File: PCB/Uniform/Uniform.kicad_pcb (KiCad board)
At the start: 2 copper layers, 156 parts, among them CON1 826629-5, CON2 Conn_01x03, U1 STM32L072KZT6

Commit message: finished board outline
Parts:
- moved R1 19.6 mm to (365.4, 230.5)
- moved R2 19.6 mm to (381.2, 230.5)
- moved R3 19.6 mm to (397.1, 230.5)
- moved R5 19.6 mm to (444.6, 230.5)
- moved R6 19.6 mm to (428.8, 230.5)
- moved C5 19.6 mm to (449.4, 234.9)
- moved CON1 19.6 mm to (366.6, 234.9)
- moved D_3_7 19.6 mm to (384.9, 234.6)
- moved D_4_10 19.6 mm to (407.9, 234.6)
- moved D_4_6 19.6 mm to (442.3, 234.6)
- moved D_4_8 19.6 mm to (430.9, 234.6)
- moved D_4_9 19.6 mm to (419.4, 234.6)
- moved S2 19.6 mm to (465.5, 231.0)
- moved R4 19.6 mm to (412.9, 230.5)
- moved D_0_10 19.6 mm to (396.4, 234.6)
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
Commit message: flipped exposed PCB side to make room for USBC pins
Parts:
- USBC1: moved to B.Cu
- moved USBC1 347.9 mm to (56.5, 107.8)
- moved CON1 343.8 mm to (42.9, 119.1), turned to 90 degrees
- moved K_0_0 26.9 mm to (71.4, 114.3)
- moved K_1_0 26.9 mm to (71.4, 133.3)
- moved K_0_11 19.1 mm to (285.8, 114.3)
- moved K_0_12 19.1 mm to (304.8, 114.3)
- moved K_0_13 19.1 mm to (328.6, 114.3)
- moved K_0_4 19.1 mm to (152.4, 114.3)
- moved K_0_6 19.1 mm to (190.5, 114.3)
- moved K_0_7 19.1 mm to (209.6, 114.3)
- moved K_0_9 19.1 mm to (247.7, 114.3)
- moved K_1_11 19.1 mm to (285.8, 133.3)
- moved K_1_12 19.1 mm to (304.8, 133.3)
- moved K_1_13 19.1 mm to (328.6, 133.3)
- moved K_1_4 19.1 mm to (152.4, 133.3)
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
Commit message: full layout first pass
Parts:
- added HOLE_M3: VAL**, keyboard_parts.pretty-master:HOLE_M3, F.Cu at (238.1, 161.9)
- added HOLE_M3: VAL**, keyboard_parts.pretty-master:HOLE_M3, F.Cu at (142.9, 161.9)
- added HOLE_M3: VAL**, keyboard_parts.pretty-master:HOLE_M3, F.Cu at (319.1, 181.0)
- added HOLE_M3: VAL**, keyboard_parts.pretty-master:HOLE_M3, F.Cu at (61.9, 181.0)
- added HOLE_M3: VAL**, keyboard_parts.pretty-master:HOLE_M3, F.Cu at (319.1, 123.8)
- added HOLE_M3: VAL**, keyboard_parts.pretty-master:HOLE_M3, F.Cu at (61.9, 123.8)
- added REF**: MountingHole_2.7mm_M2.5, MountingHole:MountingHole_2.7mm_M2.5, F.Cu at (42.8, 195.7)
- added REF**: MountingHole_2.7mm_M2.5, MountingHole:MountingHole_2.7mm_M2.5, F.Cu at (42.8, 108.7)
- moved S2 418.0 mm to (50.5, 180.9), turned to 180 degrees
- moved S1 415.1 mm to (50.5, 187.3), turned to 180 degrees
- moved C5 412.2 mm to (50.3, 131.8), turned to 180 degrees
- moved R5 406.4 mm to (42.2, 173.8)
- moved C6 402.8 mm to (54.3, 128.8), turned to 270 degrees
- moved C4 402.4 mm to (50.3, 128.8), turned to 180 degrees
- moved C3 400.8 mm to (50.3, 125.8), turned to 180 degrees
- moved U1 399.4 mm to (48.6, 142.8), turned to 90 degrees
- moved VOLT_REG1 391.5 mm to (48.6, 118.2), turned to 90 degrees
- moved C1 386.8 mm to (54.3, 119.4), turned to 90 degrees
- moved C2 385.5 mm to (42.9, 116.9), turned to 270 degrees
- moved R6 381.6 mm to (54.9, 153.8), turned to 180 degrees
- moved R4 375.6 mm to (42.2, 169.8)
- moved CON2 371.3 mm to (53.9, 196.1), turned to 270 degrees
- moved D_2_1 367.1 mm to (85.7, 154.8), turned to 90 degrees
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
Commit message: Tweaking some things
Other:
- board outline added: 301.5 x 93.4 mm
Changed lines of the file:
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@@
   )
   (gr_line (start 57.15 100.0125) (end 57.15 211.93125) (layer Dwgs.User) (width 0.15))
-  (gr_line (start 341.275 199.1) (end 341.275 105.7) (layer Dwgs.User) (width 0.15))
-  (gr_line (start 39.775 105.7) (end 341.275 105.7) (layer Dwgs.User) (width 0.15))
-  (gr_line (start 39.775 199.1) (end 39.775 105.7) (layer Dwgs.User) (width 0.15))
-  (gr_line (start 341.275 199.1) (end 39.775 199.1) (layer Dwgs.User) (width 0.15))
+  (gr_line (start 341.275 199.1) (end 341.275 105.7) (layer Edge.Cuts) (width 0.15))
+  (gr_line (start 39.775 105.7) (end 341.275 105.7) (layer Edge.Cuts) (width 0.15))
+  (gr_line (start 39.775 199.1) (end 39.775 105.7) (layer Edge.Cuts) (width 0.15))
+  (gr_line (start 341.275 199.1) (end 39.775 199.1) (layer Edge.Cuts) (width 0.15))
 )

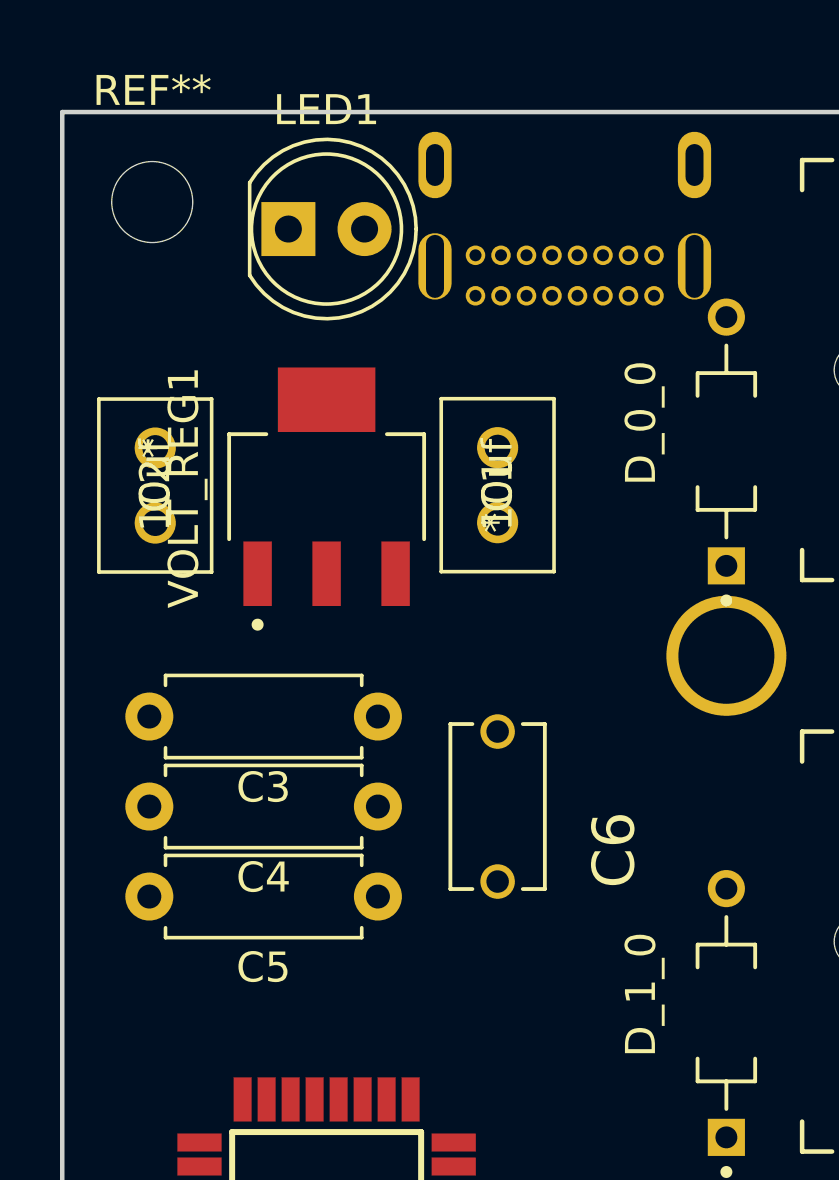
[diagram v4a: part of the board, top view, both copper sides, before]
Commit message: moved status LED to a better location
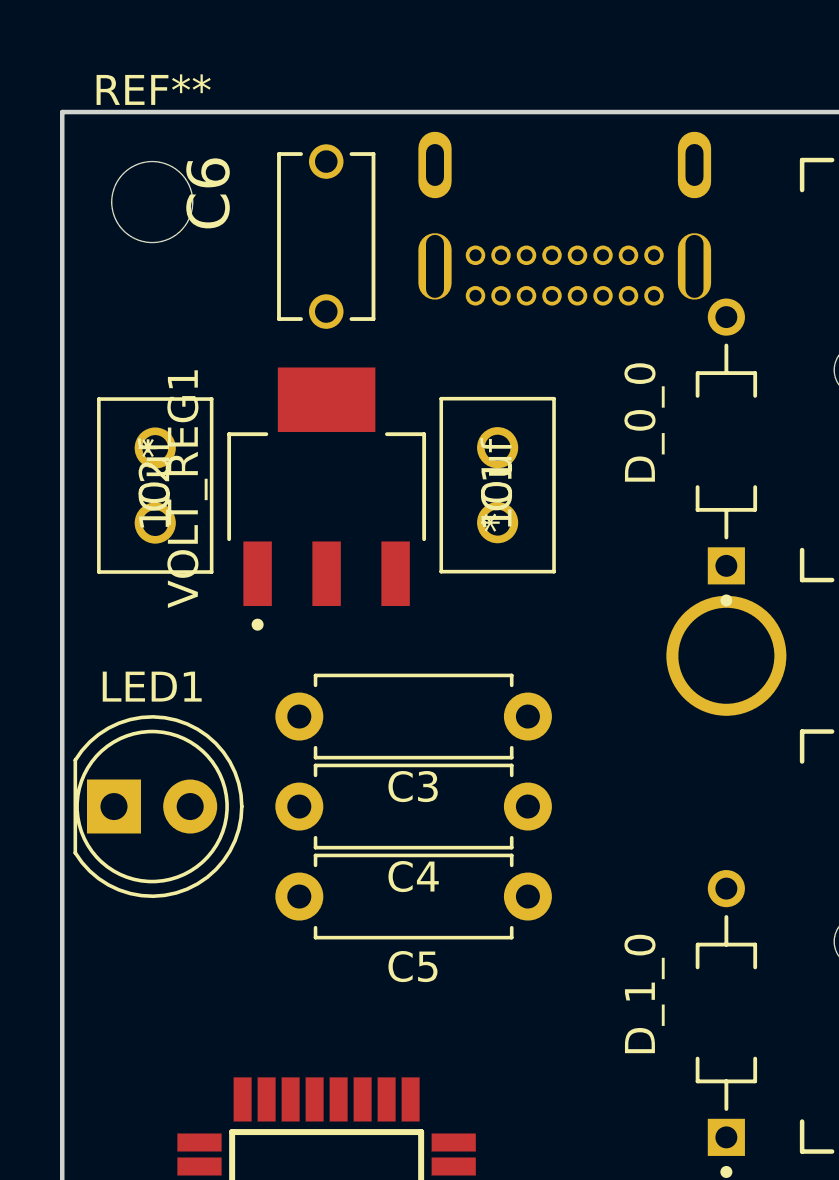
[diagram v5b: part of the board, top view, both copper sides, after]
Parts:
- moved LED1 20.1 mm to (41.5, 128.8)
- moved C6 19.8 mm to (48.6, 109.8), turned to 90 degrees
- moved C3 5.00 mm to (55.3, 125.8)
- moved C4 5.00 mm to (55.3, 128.8)
- moved C5 5.00 mm to (55.3, 131.8)
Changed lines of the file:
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@@
   )
   (module LED_THT:LED_D5.0mm_Clear (layer F.Cu)
-    (at 47.3125 109.6)
+    (at 41.5 128.85)
     (descr "LED, diameter 5.0mm, 2 pins, http://cdn-reichelt.de/documents/datenblatt/A500/LL-504BC2E-009.pdf")
     (tags "LED diameter 5.0mm 2 pins")
@@
   )
   (module RDER71H105K2M1H03A:CAP_RDER71H105K2M1H03A (layer F.Cu)
-    (at 54.2875 128.85 270)
+    (at 48.575 109.85 90)
     (fp_text reference C6 (at 1.445 -3.889 90) (layer F.SilkS)
       (effects (font (size 1.4 1.4) (thickness 0.15)))
@@
     (fp_line (start 2.75 1.575) (end -2.75 1.575) (layer F.SilkS) (width 0.127))
     (fp_line (start -2.75 -1.575) (end 2.75 -1.575) (layer F.SilkS) (width 0.127))
-    (pad 2 thru_hole circle (at 2.5 0 270) (size 1.15 1.15) (drill 0.75) (layers *.Cu *.Mask)
+    (pad 2 thru_hole circle (at 2.5 0 90) (size 1.15 1.15) (drill 0.75) (layers *.Cu *.Mask)
       (net 1 GND))
-    (pad 1 thru_hole circle (at -2.5 0 270) (size 1.15 1.15) (drill 0.75) (layers *.Cu *.Mask)
+    (pad 1 thru_hole circle (at -2.5 0 90) (size 1.15 1.15) (drill 0.75) (layers *.Cu *.Mask)
       (net 3 +3V3))
   )
   (module Resistor_THT:R_Axial_DIN0207_L6.3mm_D2.5mm_P7.62mm_Horizontal (layer F.Cu)
-    (at 50.2975 131.85 180)
+    (at 55.2975 131.85 180)
     (descr "Resistor, Axial_DIN0207 series, Axial, Horizontal, pin pitch=7.62mm, 0.25W = 1/4W, length*diameter=6.3*2.5mm^2, http://cdn-reichelt.de/documents/datenblatt/B400/1_4W%23YAG.pdf")
     (tags "Resistor Axial_DIN0207 series Axial Horizontal pin pitch 7.62mm 0.25W = 1/4W length 6.3mm diameter 2.5mm")
@@
   )
   (module Resistor_THT:R_Axial_DIN0207_L6.3mm_D2.5mm_P7.62mm_Horizontal (layer F.Cu)
-    (at 50.2975 128.85 180)
+    (at 55.2975 128.85 180)
     (descr "Resistor, Axial_DIN0207 series, Axial, Horizontal, pin pitch=7.62mm, 0.25W = 1/4W, length*diameter=6.3*2.5mm^2, http://cdn-reichelt.de/documents/datenblatt/B400/1_4W%23YAG.pdf")
     (tags "Resistor Axial_DIN0207 series Axial Horizontal pin pitch 7.62mm 0.25W = 1/4W length 6.3mm diameter 2.5mm")
@@
   )
   (module Resistor_THT:R_Axial_DIN0207_L6.3mm_D2.5mm_P7.62mm_Horizontal (layer F.Cu)
-    (at 50.2975 125.85 180)
+    (at 55.2975 125.85 180)
     (descr "Resistor, Axial_DIN0207 series, Axial, Horizontal, pin pitch=7.62mm, 0.25W = 1/4W, length*diameter=6.3*2.5mm^2, http://cdn-reichelt.de/documents/datenblatt/B400/1_4W%23YAG.pdf")
     (tags "Resistor Axial_DIN0207 series Axial Horizontal pin pitch 7.62mm 0.25W = 1/4W length 6.3mm diameter 2.5mm")

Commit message: updating project to KiCad 6.0
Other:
- net class Default removed

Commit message: Added traces for all key switches
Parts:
- moved D_1_4 0.32 mm to (142.9, 135.7)
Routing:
- net R4: track 0.00 -> 261.9 mm
- net R3: track 0.00 -> 261.9 mm
- net R2: track 0.00 -> 261.9 mm
- net R1: track 0.00 -> 257.2 mm
- net R0: track 0.00 -> 257.2 mm
- net C12: track 0.00 -> 81.1 mm
- net C11: track 0.00 -> 80.1 mm
- net C13: track 0.00 -> 78.2 mm
- net C6: track 0.00 -> 78.2 mm
- net C4: track 0.00 -> 78.2 mm
- net C9: track 0.00 -> 76.2 mm
- net C8: track 0.00 -> 76.2 mm
- net C5: track 0.00 -> 76.2 mm
- net C2: track 0.00 -> 76.2 mm
- net C10: track 0.00 -> 76.2 mm
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
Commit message: about to attempt rotating the MCU
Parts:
- moved R3 17.5 mm to (54.9, 173.8), turned to 180 degrees
- moved R4 16.0 mm to (42.2, 153.8)
- moved R2 12.7 mm to (42.2, 165.8), turned to 0 degrees
- moved R1 12.0 mm to (54.9, 169.8)
- moved R5 12.0 mm to (42.2, 161.8)
- moved S2 6.95 mm to (50.5, 187.8)
- moved S1 6.45 mm to (50.5, 180.8)
- moved R6 4.00 mm to (54.9, 157.8)
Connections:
- S1 pad 3: Net-(S1-Pad3) -> unconnected-(S1-Pad3)
- S2 pad 3: Net-(S2-Pad3) -> unconnected-(S2-Pad3)
- U1 pad 10: R4 -> C4
- U1 pad 11: C0 -> C5
- U1 pad 12: C1 -> C6
- U1 pad 13: C2 -> C7
- U1 pad 14: C3 -> C8
- U1 pad 15: C4 -> C9
- U1 pad 18: C5 -> C10
- U1 pad 19: C6 -> C11
- U1 pad 20: C7 -> C12
- U1 pad 25: C8 -> C13
- U1 pad 26: C9 -> R4
- U1 pad 27: C10 -> R3
- U1 pad 28: C11 -> R2
- U1 pad 29: C12 -> R1
- U1 pad 30: C13 -> R0
- U1 pad 6: R0 -> C0
- U1 pad 7: R1 -> C1
- U1 pad 8: R2 -> C2
- U1 pad 9: R3 -> C3
- USBC1 pad A8: Net-(USBC1-PadA8) -> unconnected-(USBC1-PadA8)
- USBC1 pad B8: Net-(USBC1-PadB8) -> unconnected-(USBC1-PadB8)
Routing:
- net C9: track 76.2 -> 276.2 mm
- net C8: track 76.2 -> 256.9 mm
- net C7: track 57.2 -> 218.4 mm
- net C6: track 78.2 -> 220.1 mm
- net C5: track 76.2 -> 199.0 mm
- net C4: track 78.2 -> 181.9 mm
- net C3: track 57.2 -> 141.8 mm
- net C2: track 76.2 -> 155.7 mm
- net RESET: track 0.00 -> 71.0 mm
- net C1: track 76.2 -> 137.4 mm
- net BOOT: track 0.00 -> 46.4 mm
- net C0: track 76.2 -> 114.2 mm
- net Net-(R3-Pad2): track 0.00 -> 28.8 mm
- net +3V3: track 0.00 -> 24.9 mm
- net Net-(R1-Pad2): track 0.00 -> 24.7 mm
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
